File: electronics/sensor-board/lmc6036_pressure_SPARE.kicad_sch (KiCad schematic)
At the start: 10 parts, among them U12 LMC6036, U16 LMC6036

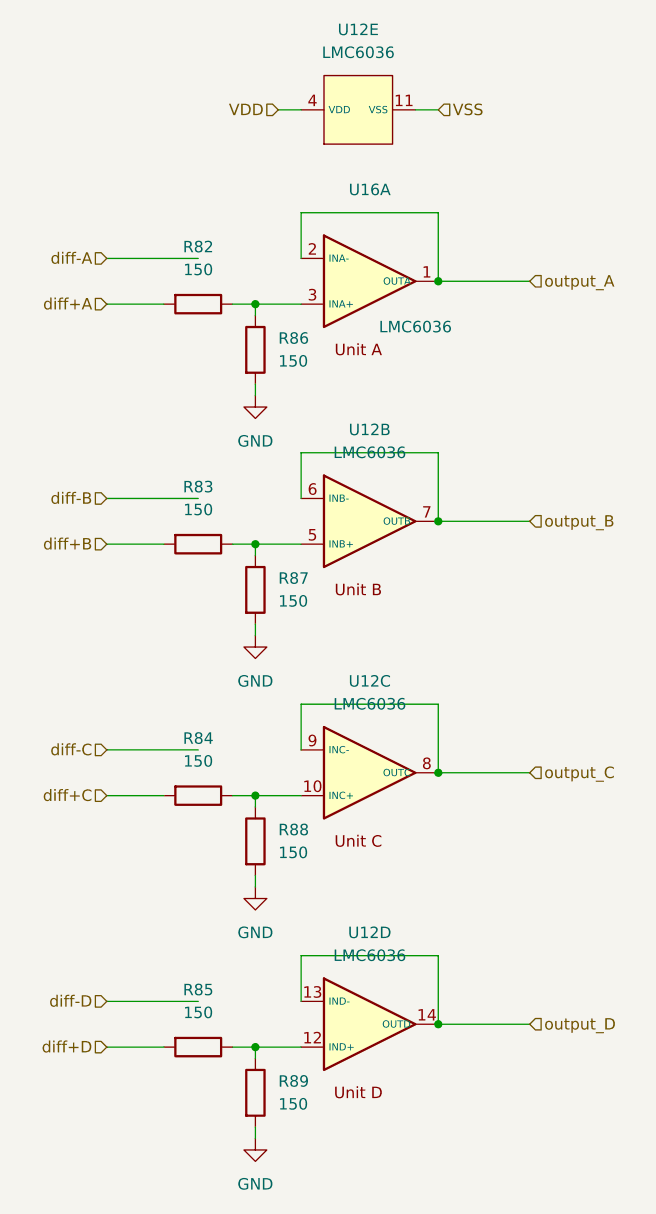
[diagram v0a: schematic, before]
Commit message: Finalized sensor-board schematic
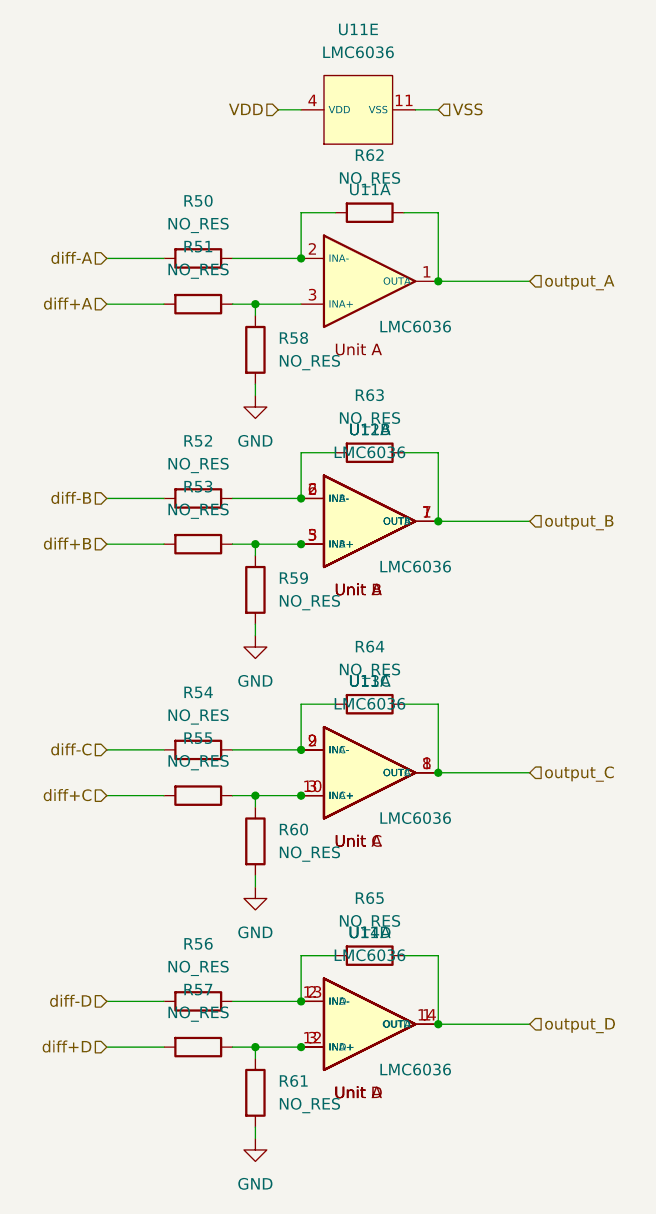
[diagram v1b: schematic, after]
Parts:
- removed R82, R83, R84, R85, R86, R87, R88, R89: 150, Resistor_SMD:R_0603_1608Metric, symbol Device:R
- removed U12, U16: LMC6036, LMC6036:SOP65P640X120-14N, symbol LMC6036_custom:LMC6036
- added R50, R51, R52, R53, R54, R55, R56, R57, R58, R59, R60, R61, R62, R63, R64, R65: NO_RES, Resistor_SMD:R_0603_1608Metric, symbol Device:R
- added U11, U12, U13, U14: LMC6036, LMC6036:SOP65P640X120-14N, symbol LMC6036_custom:LMC6036
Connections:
- net GND: now also R58.2, R59.2, R60.2, R61.2
- net VDD: now also U11.4 (VDD)
- net VSS: now also U11.11 (VSS)
- net diff+A: now also R51.2
- net diff+B: now also R53.2
- net diff+C: now also R55.2
- net diff+D: now also R57.2
- net diff-A: now also R50.2
- net diff-B: now also R52.2
- net diff-C: now also R54.2
- net diff-D: now also R56.2
- net output_A: now also R62.1, U11.1 (OUTA)
- net output_B: now also R63.1, U11.7 (OUTB), U12.1 (OUTA)
- net output_C: now also R64.1, U11.8 (OUTC), U13.1 (OUTA)
- net output_D: now also R65.1, U11.14 (OUTD), U14.1 (OUTA)
- new net: R50.1, R62.2, U11.2 (INA-)
- new net: R52.1, R63.2, U11.6 (INB-), U12.2 (INA-)
- new net: R53.1, R59.1, U11.5 (INB+), U12.3 (INA+)
- new net: R57.1, R61.1, U11.12 (IND+), U14.3 (INA+)
- new net: R56.1, R65.2, U11.13 (IND-), U14.2 (INA-)
- new net: R55.1, R60.1, U11.10 (INC+), U13.3 (INA+)
- new net: R54.1, R64.2, U11.9 (INC-), U13.2 (INA-)
- new net: R51.1, R58.1, U11.3 (INA+)

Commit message: work on sensor-board
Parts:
- removed U11, U12, U13, U14: LMC6036, LMC6036:SOP65P640X120-14N, symbol LMC6036_custom:LMC6036
- added U15: LMC6036, LMC6036:SOP65P640X120-14N, symbol LMC6036_custom:LMC6036
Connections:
- net VDD: now also U15.4 (VDD)
- net VSS: now also U15.11 (VSS)
- net output_A: now also U15.1 (OUTA)
- net output_B: now also U15.7 (OUTB)
- net output_C: now also U15.8 (OUTC)
- net output_D: now also U15.14 (OUTD)
- net at R50.1, R62.2: now also U15.2 (INA-)
- net at R52.1, R63.2: now also U15.6 (INB-)
- net at R53.1, R59.1: now also U15.5 (INB+)
- net at R57.1, R61.1: now also U15.12 (IND+)
- net at R56.1, R65.2: now also U15.13 (IND-)
- net at R55.1, R60.1: now also U15.10 (INC+)
- net at R54.1, R64.2: now also U15.9 (INC-)
- net at R51.1, R58.1: now also U15.3 (INA+)
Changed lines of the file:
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@@
   (junction (at 142.24 120.65) (diameter 0) (color 0 0 0 0))
   (junction (at 142.24 148.59) (diameter 0) (color 0 0 0 0))
-  (junction (at 147.32 60.96) (diameter 0) (color 0 0 0 0))
-  (junction (at 147.32 87.63) (diameter 0) (color 0 0 0 0))
-  (junction (at 147.32 92.71) (diameter 0) (color 0 0 0 0))
-  (junction (at 147.32 115.57) (diameter 0) (color 0 0 0 0))
-  (junction (at 147.32 120.65) (diameter 0) (color 0 0 0 0))
-  (junction (at 147.32 143.51) (diameter 0) (color 0 0 0 0))
-  (junction (at 147.32 148.59) (diameter 0) (color 0 0 0 0))
-  (junction (at 162.56 63.5) (diameter 0) (color 0 0 0 0))
-  (junction (at 162.56 90.17) (diameter 0) (color 0 0 0 0))
-  (junction (at 162.56 118.11) (diameter 0) (color 0 0 0 0))
-  (junction (at 162.56 146.05) (diameter 0) (color 0 0 0 0))
   (wire (pts (xy 125.73 60.96) (xy 132.08 60.96))
     (stroke (width 0) (type default) (color 0 0 0 0))
@@
   (symbol (lib_id "LMC6036_custom:LMC6036") (at 153.67 44.45 90) (unit 5)
     (in_bom yes) (on_board yes) (fields_autoplaced)
-    (property "Reference" "U11" (id 0) (at 153.67 35.56 90))
+    (property "Reference" "U15" (id 0) (at 153.67 35.56 90))
     (property "Value" "LMC6036" (id 1) (at 153.67 38.1 90))
     (property "Footprint" "LMC6036:SOP65P640X120-14N" (id 2) (at 153.67 42.545 0)
@@
   )
   (symbol (lib_id "LMC6036_custom:LMC6036") (at 153.67 63.5 0) (unit 1)
+    (in_bom yes) (on_board yes) (fields_autoplaced)
+    (property "Reference" "U15" (id 0) (at 154.94 53.34 0))
+    (property "Value" "LMC6036" (id 1) (at 154.94 55.88 0))
+    (property "Footprint" "LMC6036:SOP65P640X120-14N" (id 2) (at 155.575 63.5 0)
+      (effects (font (size 1.27 1.27)) hide)
+    )
+    (property "Datasheet" "" (id 3) (at 155.575 63.5 0)
+      (effects (font (size 1.27 1.27)) hide)
+    )
+    (pin "1")
+    (pin "2")
+    (pin "3")
+  )
+  (symbol (lib_id "LMC6036_custom:LMC6036") (at 153.67 90.17 0) (unit 2)
     (in_bom yes) (on_board yes)
-    (property "Reference" "U11" (id 0) (at 154.94 53.34 0))
-    (property "Value" "LMC6036" (id 1) (at 160.02 68.58 0))
-    (property "Footprint" "LMC6036:SOP65P640X120-14N" (id 2) (at 155.575 63.5 0)
-      (effects (font (size 1.27 1.27)) hide)
-    )
-    (property "Datasheet" "" (id 3) (at 155.575 63.5 0)
-      (effects (font (size 1.27 1.27)) hide)
-    )
-    (pin "1")
-    (pin "2")
-    (pin "3")
-  )
-  (symbol (lib_id "LMC6036_custom:LMC6036") (at 153.67 90.17 0) (unit 1)
-    (in_bom yes) (on_board yes)
-    (property "Reference" "U12" (id 0) (at 154.94 80.01 0))
-    (property "Value" "LMC6036" (id 1) (at 160.02 95.25 0))
-    (property "Footprint" "LMC6036:SOP65P640X120-14N" (id 2) (at 155.575 90.17 0)
-      (effects (font (size 1.27 1.27)) hide)
-    )
-    (property "Datasheet" "" (id 3) (at 155.575 90.17 0)
-      (effects (font (size 1.27 1.27)) hide)
-    )
-    (pin "1")
-    (pin "2")
-    (pin "3")
-  )
-  (symbol (lib_id "LMC6036_custom:LMC6036") (at 153.67 90.17 0) (unit 2)
-    (in_bom yes) (on_board yes) (fields_autoplaced)
-    (property "Reference" "U11" (id 0) (at 154.94 80.01 0))
-    (property "Value" "LMC6036" (id 1) (at 154.94 82.55 0))
+    (property "Reference" "U15" (id 0) (at 154.94 80.01 0))
+    (property "Value" "LMC6036" (id 1) (at 156.21 85.09 0))
     (property "Footprint" "LMC6036:SOP65P640X120-14N" (id 2) (at 155.575 90.17 0)
       (effects (font (size 1.27 1.27)) hide)
@@
   )
   (symbol (lib_id "LMC6036_custom:LMC6036") (at 153.67 118.11 0) (unit 3)
-    (in_bom yes) (on_board yes) (fields_autoplaced)
-    (property "Reference" "U11" (id 0) (at 154.94 107.95 0))
-    (property "Value" "LMC6036" (id 1) (at 154.94 110.49 0))
+    (in_bom yes) (on_board yes)
+    (property "Reference" "U15" (id 0) (at 154.94 107.95 0))
+    (property "Value" "LMC6036" (id 1) (at 154.94 113.03 0))
     (property "Footprint" "LMC6036:SOP65P640X120-14N" (id 2) (at 155.575 118.11 0)
       (effects (font (size 1.27 1.27)) hide)
@@
     (pin "9")
   )
-  (symbol (lib_id "LMC6036_custom:LMC6036") (at 153.67 118.11 0) (unit 1)
+  (symbol (lib_id "LMC6036_custom:LMC6036") (at 153.67 146.05 0) (unit 4)
     (in_bom yes) (on_board yes)
-    (property "Reference" "U13" (id 0) (at 154.94 107.95 0))
-    (property "Value" "LMC6036" (id 1) (at 160.02 123.19 0))
-    (property "Footprint" "LMC6036:SOP65P640X120-14N" (id 2) (at 155.575 118.11 0)
-      (effects (font (size 1.27 1.27)) hide)
-    )
-    (property "Datasheet" "" (id 3) (at 155.575 118.11 0)
-      (effects (font (size 1.27 1.27)) hide)
-    )
-    (pin "1")
-    (pin "2")
-    (pin "3")
-  )
-  (symbol (lib_id "LMC6036_custom:LMC6036") (at 153.67 146.05 0) (unit 4)
-    (in_bom yes) (on_board yes) (fields_autoplaced)
-    (property "Reference" "U11" (id 0) (at 154.94 135.89 0))
-    (property "Value" "LMC6036" (id 1) (at 154.94 138.43 0))
+    (property "Reference" "U15" (id 0) (at 154.94 135.89 0))
+    (property "Value" "LMC6036" (id 1) (at 154.94 142.24 0))
     (property "Footprint" "LMC6036:SOP65P640X120-14N" (id 2) (at 155.575 146.05 0)
       (effects (font (size 1.27 1.27)) hide)
@@
     (pin "14")
   )
-  (symbol (lib_id "LMC6036_custom:LMC6036") (at 153.67 146.05 0) (unit 1)
-    (in_bom yes) (on_board yes)
-    (property "Reference" "U14" (id 0) (at 154.94 135.89 0))
-    (property "Value" "LMC6036" (id 1) (at 160.02 151.13 0))
-    (property "Footprint" "LMC6036:SOP65P640X120-14N" (id 2) (at 155.575 146.05 0)
-      (effects (font (size 1.27 1.27)) hide)
-    )
-    (property "Datasheet" "" (id 3) (at 155.575 146.05 0)
-      (effects (font (size 1.27 1.27)) hide)
-    )
-    (pin "1")
-    (pin "2")
-    (pin "3")
-  )
 )
